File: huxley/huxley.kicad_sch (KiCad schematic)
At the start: 2 parts, among them U6 NVT2010PW_118

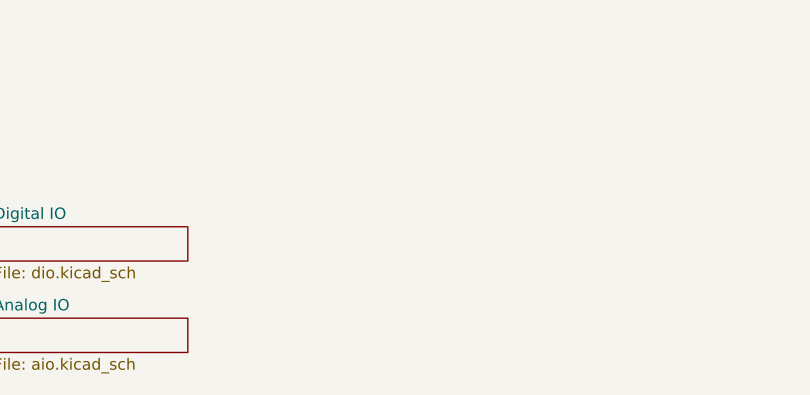
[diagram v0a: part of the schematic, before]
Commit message: added analog chip schematics and connector footprints
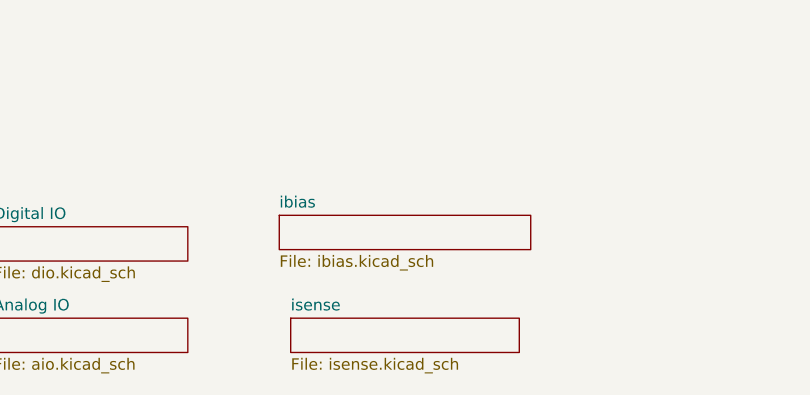
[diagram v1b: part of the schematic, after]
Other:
- added sheet ibias (ibias.kicad_sch)
- added sheet isense (isense.kicad_sch)
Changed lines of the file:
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@@
+	)
+	(sheet
+		(at 93.98 176.53)
+		(size 25.4 3.81)
+		(fields_autoplaced yes)
+		(stroke
+			(width 0.1524)
+			(type solid)
+		)
+		(fill
+			(color 0 0 0 0.0000)
+		)
+		(property "Sheetname" "isense"
+			(at 93.98 175.8184 0)
+			(effects
+				(font
+					(size 1.27 1.27)
+				)
+				(justify left bottom)
+			)
+		)
+		(property "Sheetfile" "isense.kicad_sch"
+			(at 93.98 180.9246 0)
+			(effects
+				(font
+					(size 1.27 1.27)
+				)
+				(justify left top)
+			)
+		)
+		(instances
+			(project "huxley"
+				(path "/c6103430-c27a-4e90-8e2e-9404255f5ee3"
+					(page "6")
+				)
+			)
+		)
 	)
 	(sheet
@@
 				)
 			)
+		)
+	)
+	(sheet
+		(at 92.71 165.1)
+		(size 27.94 3.81)
+		(fields_autoplaced yes)
+		(stroke
+			(width 0.1524)
+			(type solid)
+		)
+		(fill
+			(color 0 0 0 0.0000)
+		)
+		(property "Sheetname" "ibias"
+			(at 92.71 164.3884 0)
+			(effects
+				(font
+					(size 1.27 1.27)
+				)
+				(justify left bottom)
+			)
+		)
+		(property "Sheetfile" "ibias.kicad_sch"
+			(at 92.71 169.4946 0)
+			(effects
+				(font
+					(size 1.27 1.27)
+				)
+				(justify left top)
+			)
+		)
+		(instances
+			(project "huxley"
+				(path "/c6103430-c27a-4e90-8e2e-9404255f5ee3"
+					(page "5")
+				)
+			)

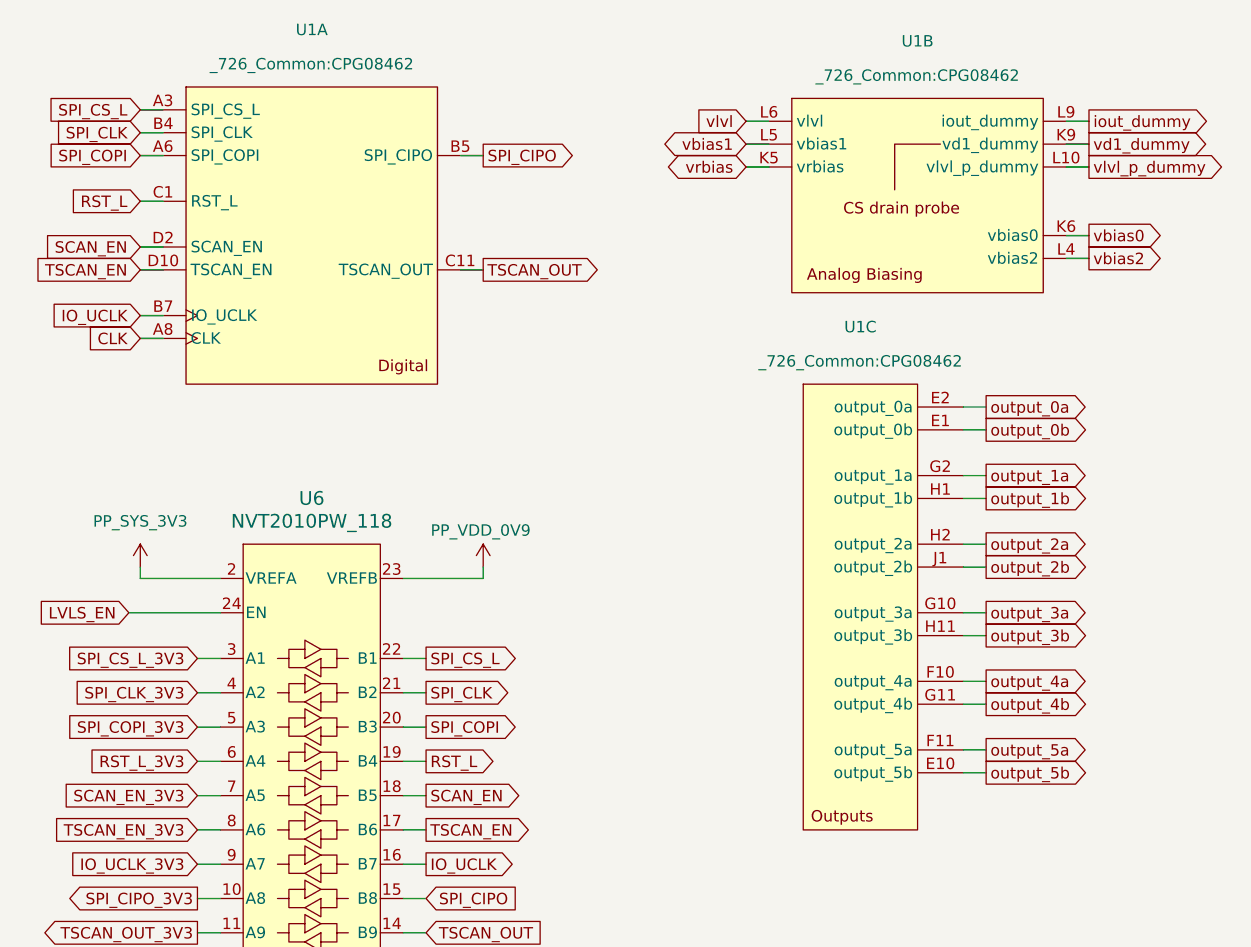
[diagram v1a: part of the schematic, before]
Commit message: updated footprints
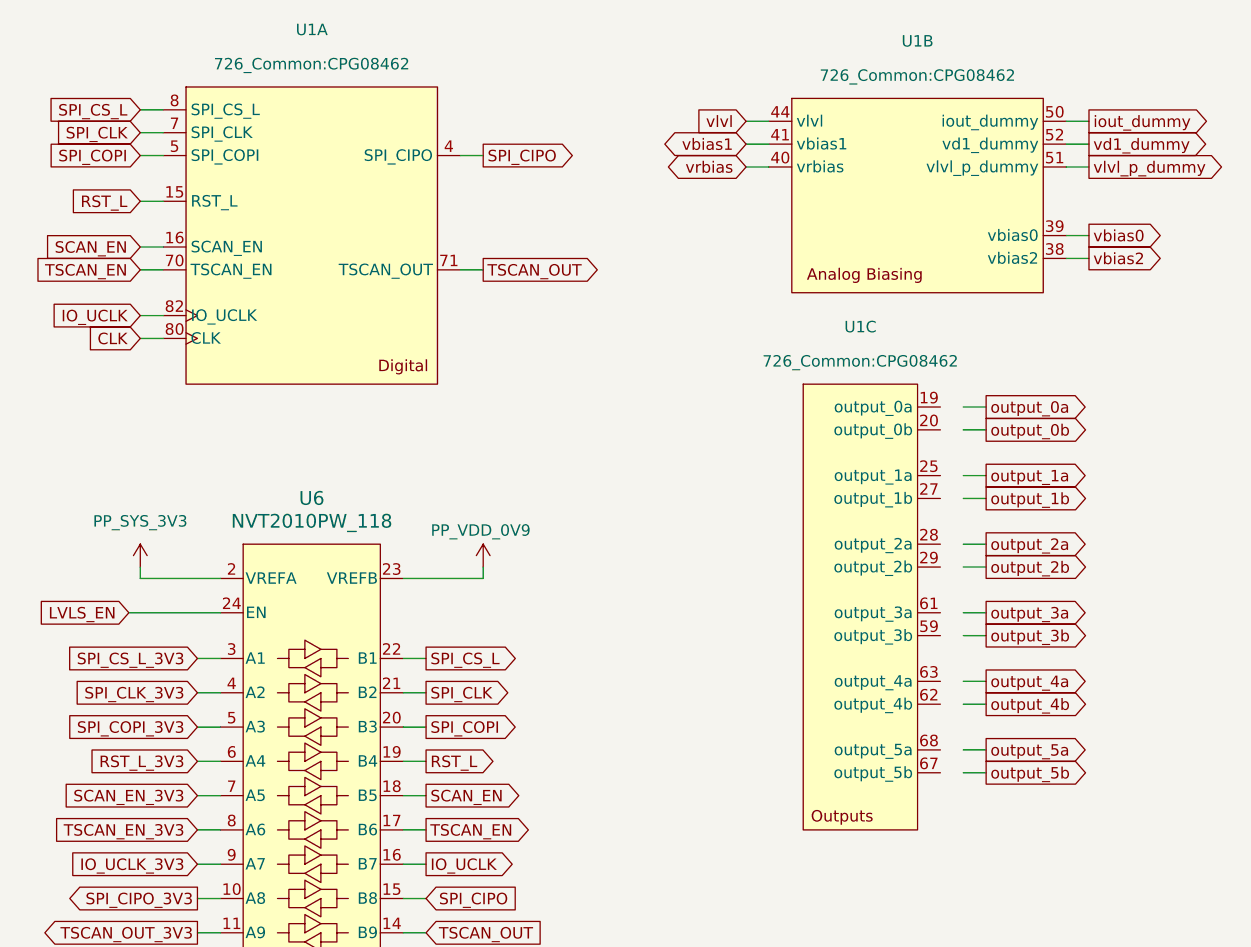
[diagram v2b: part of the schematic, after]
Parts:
- U1: footprint _726_Common:CPG08462 -> 726_Common:CPG08462
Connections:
- net CLK: now also U1.80 (CLK); no longer U1.A8 (CLK)
- net IO_UCLK: now also U1.82 (IO_UCLK); no longer U1.B7 (IO_UCLK)
- net RST_L: now also U1.15 (RST_L); no longer U1.C1 (RST_L)
- net SCAN_EN: now also U1.16 (SCAN_EN); no longer U1.D2 (SCAN_EN)
- net SPI_CIPO: now also U1.4 (SPI_CIPO); no longer U1.B5 (SPI_CIPO)
- net SPI_CLK: now also U1.7 (SPI_CLK); no longer U1.B4 (SPI_CLK)
- net SPI_COPI: now also U1.5 (SPI_COPI); no longer U1.A6 (SPI_COPI)
- net SPI_CS_L: now also U1.8 (SPI_CS_L); no longer U1.A3 (SPI_CS_L)
- net TSCAN_EN: now also U1.70 (TSCAN_EN); no longer U1.D10 (TSCAN_EN)
- net TSCAN_OUT: now also U1.71 (TSCAN_OUT); no longer U1.C11 (TSCAN_OUT)
- net iout_dummy: now also U1.50 (iout_dummy); no longer U1.L9 (iout_dummy)
- net output_0a: no longer U1.E2 (output_0a)
- net output_0b: no longer U1.E1 (output_0b)
- net output_1a: no longer U1.G2 (output_1a)
- net output_1b: no longer U1.H1 (output_1b)
- net output_2a: no longer U1.H2 (output_2a)
- net output_2b: no longer U1.J1 (output_2b)
- net output_3a: no longer U1.G10 (output_3a)
- net output_3b: no longer U1.H11 (output_3b)
- net output_4a: no longer U1.F10 (output_4a)
- net output_4b: no longer U1.G11 (output_4b)
- net output_5a: no longer U1.F11 (output_5a)
- net output_5b: no longer U1.E10 (output_5b)
- net vbias0: now also U1.39 (vbias0); no longer U1.K6 (vbias0)
- net vbias1: now also U1.41 (vbias1); no longer U1.L5 (vbias1)
- net vbias2: now also U1.38 (vbias2); no longer U1.L4 (vbias2)
- net vd1_dummy: now also U1.52 (vd1_dummy); no longer U1.K9 (vd1_dummy)
- net vlvl: now also U1.44 (vlvl); no longer U1.L6 (vlvl)
- net vlvl_p_dummy: now also U1.51 (vlvl_p_dummy); no longer U1.L10 (vlvl_p_dummy)
- net vrbias: now also U1.40 (vrbias); no longer U1.K5 (vrbias)
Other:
- moved on the sheet: U1C

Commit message: layout_1003
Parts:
- added J5: SMA_RF2-04A-T-00-50-G, 726_footprints:CONN_RF2-04A-T-00-50-G_ADM, symbol _PHASE:SMA_RF2-04A-T-00-50-G
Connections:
- net CLK: now also J5.1
- net GND: now also J5.2, J5.3 (Ext), J5.4 (Ext), J5.5 (Ext)
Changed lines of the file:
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@@
+	(wire
+		(pts
+			(xy 128.27 128.27) (xy 132.08 128.27)
+		)
+		(stroke
+			(width 0)
+			(type default)
+		)
+	)
 	(wire
 		(pts
@@
 	(wire
 		(pts
+			(xy 115.57 128.27) (xy 123.19 128.27)
+		)
+		(stroke
+			(width 0)
+			(type default)
+		)
+	)
+	(wire
+		(pts
 			(xy 146.05 39.37) (xy 143.51 39.37)
 		)
@@
 			(width 0)
 			(type default)
+		)
+	)
+	(label "CLK"
+		(at 115.57 128.27 0)
+		(fields_autoplaced yes)
+		(effects
+			(font
+				(size 1.27 1.27)
+			)
+			(justify left bottom)
 		)
 	)
@@
 					(unit 1)
 				)
+			)
+		)
+	)
+	(symbol
+		(lib_id "power:GND")
+		(at 132.08 128.27 0)
+		(unit 1)
+		(exclude_from_sim no)
+		(in_bom yes)
+		(on_board yes)
+		(dnp no)
+		(fields_autoplaced yes)
+		(property "Reference" "#PWR016"
+			(at 132.08 134.62 0)
+			(effects
+				(font
+					(size 1.27 1.27)
+				)
+				(hide yes)
+			)
+		)
+		(property "Value" "GND"
+			(at 132.08 133.35 0)
+			(effects
+				(font
+					(size 1.27 1.27)
+				)
+			)
+		)
+		(property "Footprint" ""
+			(at 132.08 128.27 0)
+			(effects
+				(font
+					(size 1.27 1.27)
+				)
+				(hide yes)
+			)
+		)
+		(property "Datasheet" ""
+			(at 132.08 128.27 0)
+			(effects
+				(font
+					(size 1.27 1.27)
+				)
+				(hide yes)
+			)
+		)
+		(property "Description" "Power symbol creates a global label with name \"GND\" , ground"
+			(at 132.08 128.27 0)
+			(effects
+				(font
+					(size 1.27 1.27)
+				)
+				(hide yes)
+			)
+		)
+		(pin "1"
+		)
+		(instances
+			(project "huxley"
+				(path "/c6103430-c27a-4e90-8e2e-9404255f5ee3"
+					(reference "#PWR016")
+					(unit 1)
+				)
+			)
+		)
+	)
+	(symbol
+		(lib_id "_PHASE:SMA_RF2-04A-T-00-50-G")
+		(at 113.03 123.19 0)
+		(unit 1)
+		(exclude_from_sim no)
+		(in_bom yes)
+		(on_board yes)
+		(dnp no)
+		(fields_autoplaced yes)
+		(property "Reference" "J5"
+			(at 121.666 126.492 0)
+			(effects
+				(font
+					(size 1.524 1.524)
+				)
+			)
+		)
+		(property "Value" "SMA_RF2-04A-T-00-50-G"
+			(at 125.2104 124.46 0)
+			(effects
+				(font
+					(size 1.524 1.524)
+				)
+			)
+		)
+		(property "Footprint" "726_footprints:CONN_RF2-04A-T-00-50-G_ADM"
+			(at 113.03 123.19 0)
+			(effects
+				(font
+					(size 1.27 1.27)
+					(italic yes)
+				)
+				(hide yes)
+			)
+		)
+		(property "Datasheet" "112404"
+			(at 113.03 123.19 0)
+			(effects
+				(font
+					(size 1.27 1.27)
+					(italic yes)
+				)
+				(hide yes)
+			)
+		)
+		(property "Description" ""
+			(at 113.03 123.19 0)
+			(effects
+				(font
+					(size 1.27 1.27)
+				)
+				(hide yes)
+			)
+		)
+		(pin "2"
+		)
+		(pin "3"
+		)
+		(pin "1"
+		)
+		(pin "5"
+		)
+		(pin "4"
+		)
+		(instances
+			(project "huxley"
+				(path "/c6103430-c27a-4e90-8e2e-9404255f5ee3"
+					(reference "J5")
+					(unit 1)
+				)

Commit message: layout_1003_2
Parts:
- U1: footprint 726_Common:CPG08462 -> 0_726_footprints:CPG08462_Full; symbol _PHASE:PHASEIC_SOCKET -> 0_PHASE:PHASEIC_SOCKET
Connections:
- net CLK: now also U1.A8 (CLK); no longer U1.80 (CLK)
- net IO_UCLK: now also U1.B7 (IO_UCLK); no longer U1.82 (IO_UCLK)
- net RST_L: now also U1.C1 (RST_L); no longer U1.15 (RST_L)
- net SCAN_EN: now also U1.D2 (SCAN_EN); no longer U1.16 (SCAN_EN)
- net SPI_CIPO: now also U1.B5 (SPI_CIPO); no longer U1.4 (SPI_CIPO)
- net SPI_CLK: now also U1.B4 (SPI_CLK); no longer U1.7 (SPI_CLK)
- net SPI_COPI: now also U1.A6 (SPI_COPI); no longer U1.5 (SPI_COPI)
- net SPI_CS_L: now also U1.A3 (SPI_CS_L); no longer U1.8 (SPI_CS_L)
- net TSCAN_EN: now also U1.D10 (TSCAN_EN); no longer U1.70 (TSCAN_EN)
- net TSCAN_OUT: now also U1.C11 (TSCAN_OUT); no longer U1.71 (TSCAN_OUT)
- net iout_dummy: now also U1.L9 (iout_dummy); no longer U1.50 (iout_dummy)
- net output_0a: now also U1.E2 (output_0a)
- net output_0b: now also U1.E1 (output_0b)
- net output_1a: now also U1.G2 (output_1a)
- net output_1b: now also U1.H1 (output_1b)
- net output_2a: now also U1.H2 (output_2a)
- net output_2b: now also U1.J1 (output_2b)
- net output_3a: now also U1.G10 (output_3a)
- net output_3b: now also U1.H11 (output_3b)
- net output_4a: now also U1.F10 (output_4a)
- net output_4b: now also U1.G11 (output_4b)
- net output_5a: now also U1.F11 (output_5a)
- net output_5b: now also U1.E10 (output_5b)
- net vbias0: now also U1.K6 (vbias0); no longer U1.39 (vbias0)
- net vbias1: now also U1.L5 (vbias1); no longer U1.41 (vbias1)
- net vbias2: now also U1.L4 (vbias2); no longer U1.38 (vbias2)
- net vd1_dummy: now also U1.K9 (vd1_dummy); no longer U1.52 (vd1_dummy)
- net vlvl: now also U1.L6 (vlvl); no longer U1.44 (vlvl)
- net vlvl_p_dummy: now also U1.L10 (vlvl_p_dummy); no longer U1.51 (vlvl_p_dummy)
- net vrbias: now also U1.K5 (vrbias); no longer U1.40 (vrbias)
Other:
- moved on the sheet: U1C

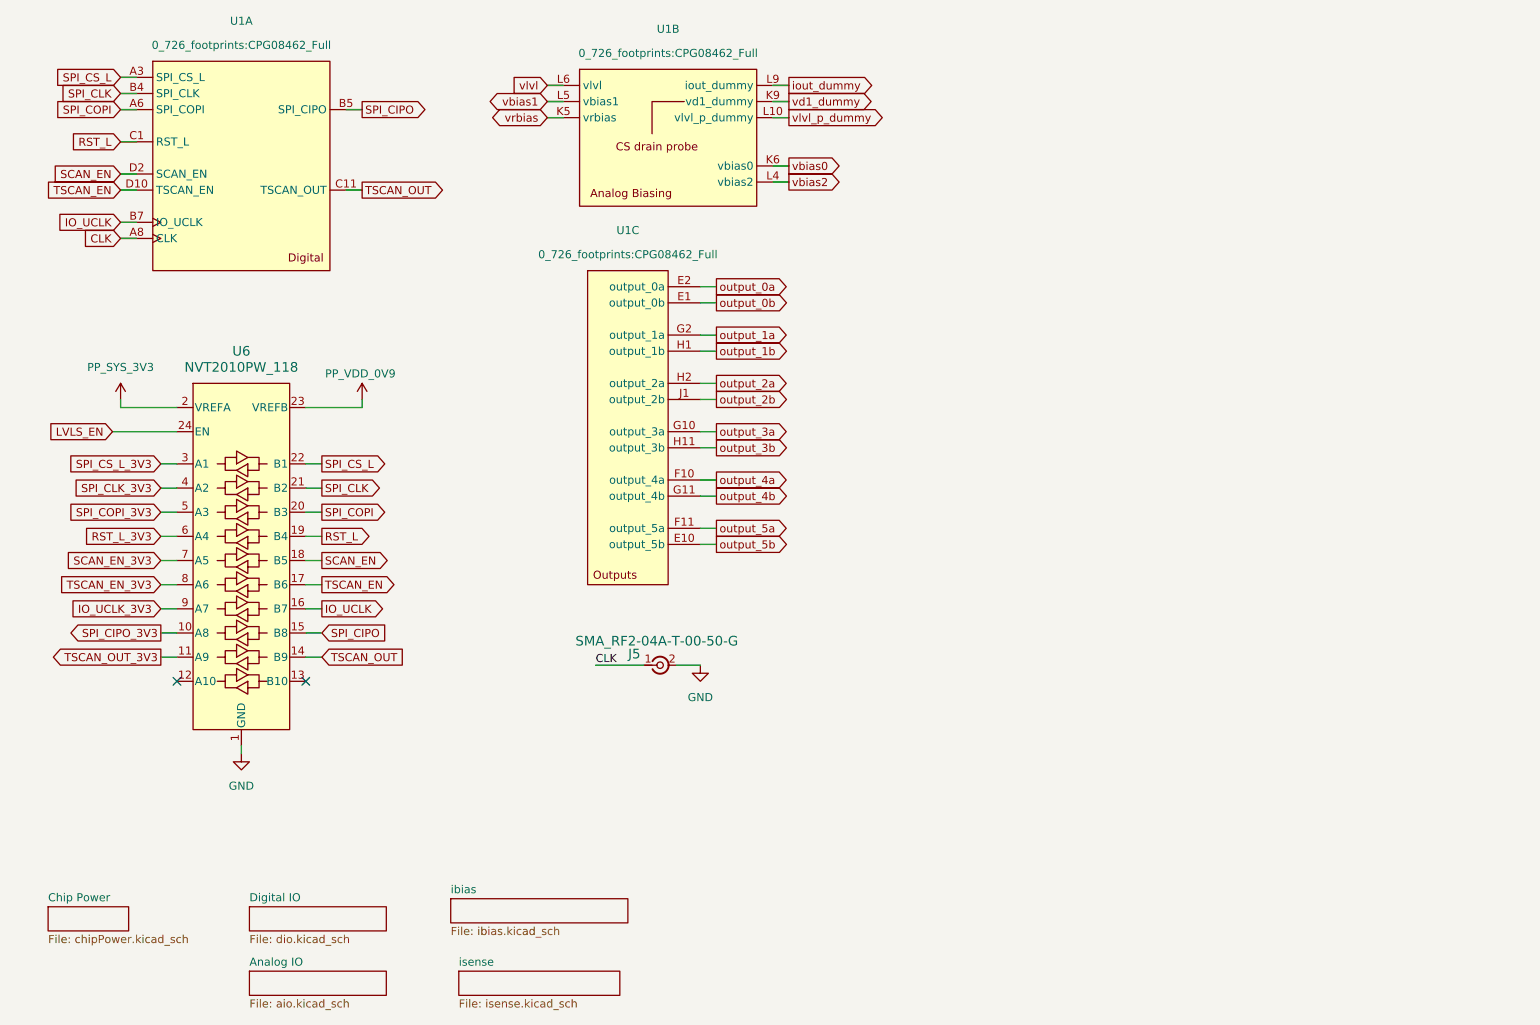
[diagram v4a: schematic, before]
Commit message: reorganized pin assignment to level shifter; matched 3V3 power net name; minor schematic cleanup
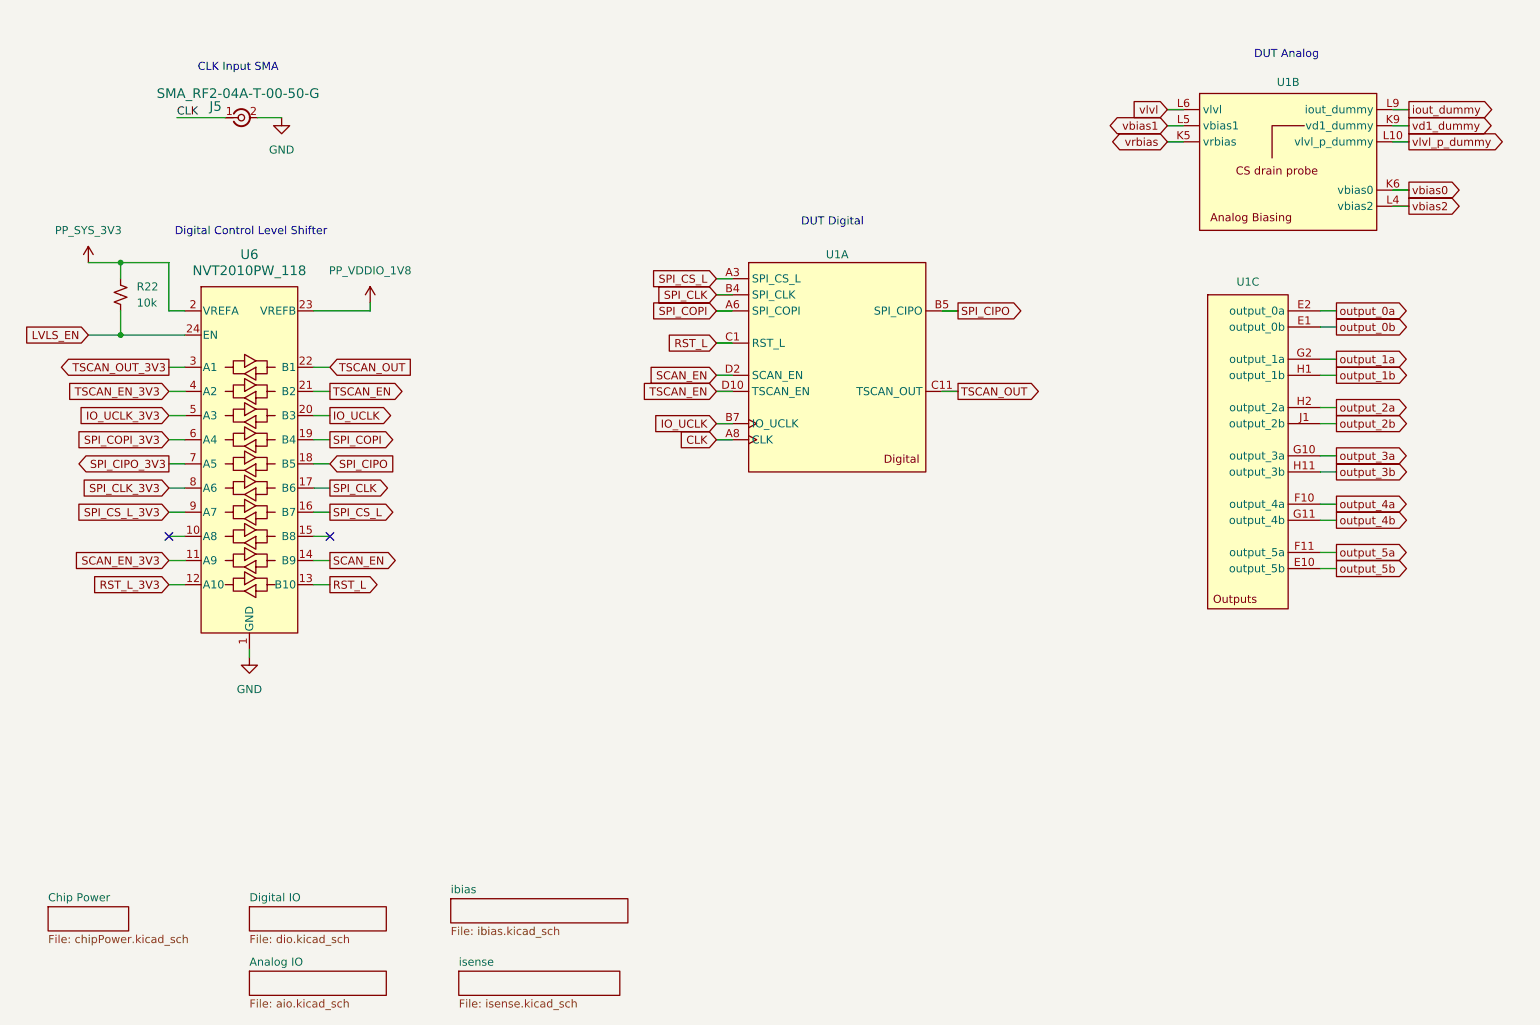
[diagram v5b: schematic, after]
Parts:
- added R22: 10k, Resistor_SMD:R_0603_1608Metric, symbol Device:R_Small_US
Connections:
- net IO_UCLK: now also U6.20 (B3); no longer U6.16 (B7)
- net IO_UCLK_3V3: now also U6.5 (A3); no longer U6.9 (A7)
- net LVLS_EN: now also R22.2
- net PP_SYS_3V3: now also R22.1
- net RST_L: now also U6.13 (B10); no longer U6.19 (B4)
- net RST_L_3V3: now also U6.12 (A10); no longer U6.6 (A4)
- net SCAN_EN: now also U6.14 (B9); no longer U6.18 (B5)
- net SCAN_EN_3V3: now also U6.11 (A9); no longer U6.7 (A5)
- net SPI_CIPO: now also U6.18 (B5); no longer U6.15 (B8)
- net SPI_CIPO_3V3: now also U6.7 (A5); no longer U6.10 (A8)
- net SPI_CLK: now also U6.17 (B6); no longer U6.21 (B2)
- net SPI_CLK_3V3: now also U6.8 (A6); no longer U6.4 (A2)
- net SPI_COPI: now also U6.19 (B4); no longer U6.20 (B3)
- net SPI_COPI_3V3: now also U6.6 (A4); no longer U6.5 (A3)
- net SPI_CS_L: now also U6.16 (B7); no longer U6.22 (B1)
- net SPI_CS_L_3V3: now also U6.9 (A7); no longer U6.3 (A1)
- net TSCAN_EN: now also U6.21 (B2); no longer U6.17 (B6)
- net TSCAN_EN_3V3: now also U6.4 (A2); no longer U6.8 (A6)
- net TSCAN_OUT: now also U6.22 (B1); no longer U6.14 (B9)
- net TSCAN_OUT_3V3: now also U6.3 (A1); no longer U6.11 (A9)
- net PP_VDD_0V9 renamed PP_VDDIO_1V8
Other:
- note added: "CLK Input SMA"
- note added: "DUT Analog"
- note added: "DUT Digital"
- note added: "Digital Control Level Shifter"
- moved on the sheet: J5, U1A, U1B, U1C, U6
